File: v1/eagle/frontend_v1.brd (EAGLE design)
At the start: 100 x 50 mm, 57 parts, among them IC1 TINY24/44/84-SSU, IC2 AD5339MSOP8, IC3 LM4041A12DCK, Q10 TIP42C, Q9 TIP41C, T3 TIP35CVERTICAL, T4 TIP35CVERTICAL, U2 LM35DT, U3 LM35DT

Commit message: minor changes
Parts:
- R1, R16, R17, R35: device rcl:R2010 -> rcl:R2512
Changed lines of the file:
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@@
 </autorouter>
 <elements>
-<element name="R1" library="rcl" package="R2010" value="0.1" x="66.5" y="30.5" smashed="yes" rot="R180">
+<element name="R1" library="rcl" package="R2512" value="0.1" x="66.5" y="30.5" smashed="yes" rot="R180">
 <attribute name="NAME" x="65.675" y="28.845" size="1.27" layer="25" rot="R180"/>
 </element>
@@
 <attribute name="NAME" x="67.92" y="6.7048" size="1.27" layer="25" ratio="10"/>
 </element>
-<element name="R16" library="rcl" package="R2010" value="0.1" x="76.25" y="5" rot="R180"/>
-<element name="R17" library="rcl" package="R2010" value="0.1" x="30.25" y="4.75" rot="R180"/>
+<element name="R16" library="rcl" package="R2512" value="0.1" x="76.25" y="5" smashed="yes" rot="R180">
+<attribute name="NAME" x="78.79" y="3.095" size="1.27" layer="25" rot="R180"/>
+</element>
+<element name="R17" library="rcl" package="R2512" value="0.1" x="30.25" y="4.75" smashed="yes" rot="R180">
+<attribute name="NAME" x="32.79" y="2.845" size="1.27" layer="25" rot="R180"/>
+</element>
 <element name="T5" library="transistor" package="SOT23-BEC" value="" x="42.46" y="33.5" smashed="yes" rot="R270">
 <attribute name="NAME" x="38.845" y="32.865" size="1.27" layer="25"/>
@@
 <element name="U2" library="parts" package="TO220AV" value="LM35DT" x="27" y="14.25" rot="R180"/>
 <element name="U3" library="parts" package="TO220AV" value="LM35DT" x="73" y="14.25" rot="R180"/>
-<element name="R35" library="rcl" package="R2010" value="0.1" x="66.5" y="35.25" smashed="yes" rot="R180">
+<element name="R35" library="rcl" package="R2512" value="0.1" x="66.5" y="35.25" smashed="yes" rot="R180">
 <attribute name="NAME" x="66.425" y="38.095" size="1.27" layer="25" rot="R180"/>
 </element>
@@
 <contactref element="O2" pad="8"/>
 <contactref element="C22" pad="1"/>
-<wire x1="64.3" y1="30.5" x2="64.3" y2="35.25" width="1.5" layer="1"/>
-<wire x1="64.3" y1="35.25" x2="65.775" y2="36.725" width="1.5" layer="1"/>
-<wire x1="65.775" y1="36.725" x2="71.525" y2="42.475" width="1.5" layer="1"/>
-<wire x1="71.525" y1="42.475" x2="73.13" y2="44.08" width="1.5" layer="1"/>
-<wire x1="73.13" y1="44.08" x2="73.13" y2="44.5" width="1.5" layer="1"/>
+<wire x1="63.7" y1="30.5" x2="63.7" y2="35.25" width="2" layer="1"/>
+<wire x1="65.775" y1="36.725" x2="71.525" y2="42.475" width="2" layer="1"/>
+<wire x1="71.525" y1="42.475" x2="73.13" y2="44.08" width="2" layer="1"/>
+<wire x1="73.13" y1="44.08" x2="73.13" y2="44.5" width="2" layer="1"/>
 <wire x1="59.46" y1="30.46" x2="59.5" y2="30.5" width="1.5" layer="1"/>
-<wire x1="59.5" y1="30.5" x2="64.3" y2="30.5" width="1.5" layer="1"/>
+<wire x1="59.5" y1="30.5" x2="63.7" y2="30.5" width="2" layer="1"/>
 <wire x1="33.31" y1="29.44" x2="35.75" y2="31.88" width="0.4" layer="16"/>
 <wire x1="35.75" y1="31.88" x2="35.75" y2="32.05" width="0.4" layer="16"/>
@@
 <wire x1="47.25" y1="37" x2="51.45" y2="41.2" width="0.4" layer="1"/>
 <wire x1="51.45" y1="41.2" x2="59.5" y2="41.2" width="0.4" layer="1"/>
+<wire x1="65.775" y1="36.725" x2="64.3" y2="35.25" width="2" layer="1"/>
+<wire x1="64.3" y1="35.25" x2="63.7" y2="35.25" width="1.5" layer="1"/>
 </signal>
 <signal name="VREF">
@@
 <contactref element="HDR_OUT" pad="3"/>
 <contactref element="R5" pad="1"/>
-<wire x1="69.65" y1="5" x2="74.05" y2="5" width="1.5" layer="1"/>
-<wire x1="24.15" y1="4.75" x2="28.05" y2="4.75" width="1.5" layer="1"/>
-<wire x1="96.5" y1="11.46" x2="87.04" y2="2" width="1.5" layer="1"/>
-<wire x1="87.04" y1="2" x2="74.25" y2="2" width="1.5" layer="1"/>
-<wire x1="74.25" y1="2" x2="30.5" y2="2" width="1.5" layer="1"/>
-<wire x1="30.5" y1="2" x2="28.05" y2="4.45" width="1.5" layer="1"/>
-<wire x1="28.05" y1="4.45" x2="28.05" y2="4.75" width="1.5" layer="1"/>
-<wire x1="74.05" y1="5" x2="74.25" y2="4.8" width="1.5" layer="1"/>
-<wire x1="74.25" y1="4.8" x2="74.25" y2="2" width="1.5" layer="1"/>
+<wire x1="69.65" y1="5" x2="73.45" y2="5" width="2" layer="1"/>
+<wire x1="24.15" y1="4.75" x2="27.45" y2="4.75" width="2" layer="1"/>
+<wire x1="96.5" y1="11.46" x2="87.04" y2="1.75" width="2" layer="1"/>
+<wire x1="87.04" y1="1.75" x2="73.5" y2="1.75" width="2" layer="1"/>
+<wire x1="73.5" y1="1.75" x2="30.75" y2="1.75" width="2" layer="1"/>
+<wire x1="30.75" y1="1.75" x2="28.05" y2="4.45" width="2" layer="1"/>
+<wire x1="28.05" y1="4.45" x2="27.45" y2="4.75" width="1.5" layer="1"/>
 <wire x1="28.25" y1="41.2" x2="26.7" y2="41.2" width="0.4" layer="1"/>
 <wire x1="26.7" y1="41.2" x2="23.5" y2="38" width="0.4" layer="1"/>
@@
 <wire x1="19.3" y1="30.05" x2="19" y2="29.75" width="0.4" layer="16"/>
 <wire x1="19" y1="29.75" x2="19" y2="9.25" width="0.4" layer="16"/>
+<wire x1="73.45" y1="5" x2="73.5" y2="4.95" width="1.5" layer="1"/>
+<wire x1="73.5" y1="4.95" x2="73.5" y2="1.75" width="2" layer="1"/>
 </signal>
 <signal name="N$29">
@@
 <contactref element="T4" pad="P3"/>
 <contactref element="R16" pad="1"/>
-<wire x1="78.45" y1="10.55" x2="78.45" y2="5" width="1.5" layer="1"/>
+<wire x1="78.45" y1="10.55" x2="79.05" y2="9.95" width="2" layer="1"/>
+<wire x1="79.05" y1="9.95" x2="79.05" y2="5" width="2" layer="1"/>
 </signal>
 <signal name="N$19">
 <contactref element="T3" pad="P3"/>
 <contactref element="R17" pad="1"/>
-<wire x1="32.45" y1="4.75" x2="32.45" y2="10.55" width="1.5" layer="1"/>
+<wire x1="33.05" y1="4.75" x2="33.05" y2="9.95" width="1.5" layer="1"/>
+<wire x1="33.05" y1="9.95" x2="32.45" y2="10.55" width="1.5" layer="1"/>
 </signal>
 <signal name="N$15">
@@
 <contactref element="R12" pad="1"/>
 <contactref element="T4" pad="P2"/>
-<wire x1="68.7" y1="35.25" x2="68.7" y2="33.25" width="1.5" layer="1"/>
-<wire x1="68.7" y1="33.25" x2="68.7" y2="30.5" width="1.5" layer="1"/>
-<wire x1="73" y1="10.55" x2="69.95" y2="7.5" width="1.5" layer="1"/>
-<wire x1="69.95" y1="7.5" x2="66.25" y2="7.5" width="1.5" layer="1"/>
-<wire x1="66.25" y1="7.5" x2="64.5" y2="9.25" width="1.5" layer="1"/>
-<wire x1="64.5" y1="9.25" x2="64.5" y2="20.25" width="1.5" layer="1"/>
-<wire x1="64.5" y1="20.25" x2="64.5" y2="23.5" width="1.5" layer="1"/>
-<wire x1="64.5" y1="23.5" x2="68.7" y2="27.7" width="1.5" layer="1"/>
-<wire x1="68.7" y1="27.7" x2="68.7" y2="30.5" width="1.5" layer="1"/>
-<wire x1="27" y1="10.55" x2="23.95" y2="7.5" width="1.5" layer="1"/>
-<wire x1="23.95" y1="7.5" x2="20" y2="7.5" width="1.5" layer="1"/>
-<wire x1="20" y1="7.5" x2="18.5" y2="9" width="1.5" layer="1"/>
-<wire x1="18.5" y1="9" x2="18.5" y2="20.25" width="1.5" layer="1"/>
-<wire x1="18.5" y1="20.25" x2="64.5" y2="20.25" width="1.5" layer="1"/>
-<wire x1="72.55" y1="33.25" x2="68.7" y2="33.25" width="0.4" layer="1"/>
+<wire x1="73" y1="10.55" x2="69.95" y2="7.5" width="2" layer="1"/>
+<wire x1="69.95" y1="7.5" x2="66.25" y2="7.5" width="2" layer="1"/>
+<wire x1="66.25" y1="7.5" x2="64.5" y2="9.25" width="2" layer="1"/>
+<wire x1="64.5" y1="9.25" x2="64.5" y2="20.25" width="2" layer="1"/>
+<wire x1="64.5" y1="20.25" x2="64.5" y2="23.5" width="2" layer="1"/>
+<wire x1="27" y1="10.55" x2="23.95" y2="7.5" width="2" layer="1"/>
+<wire x1="23.95" y1="7.5" x2="20" y2="7.5" width="2" layer="1"/>
+<wire x1="20" y1="7.5" x2="18.5" y2="9" width="2" layer="1"/>
+<wire x1="18.5" y1="9" x2="18.5" y2="20.25" width="2" layer="1"/>
+<wire x1="18.5" y1="20.25" x2="64.5" y2="20.25" width="2" layer="1"/>
+<wire x1="69.3" y1="35.25" x2="69.3" y2="33.25" width="2" layer="1"/>
+<wire x1="69.3" y1="33.25" x2="69.3" y2="30.5" width="2" layer="1"/>
+<wire x1="72.55" y1="33.25" x2="69.3" y2="33.25" width="0.3" layer="1"/>
+<wire x1="64.5" y1="23.5" x2="69.3" y2="28.3" width="2" layer="1"/>
+<wire x1="69.3" y1="28.3" x2="69.3" y2="30.5" width="2" layer="1"/>
 </signal>
 <signal name="ADC1">

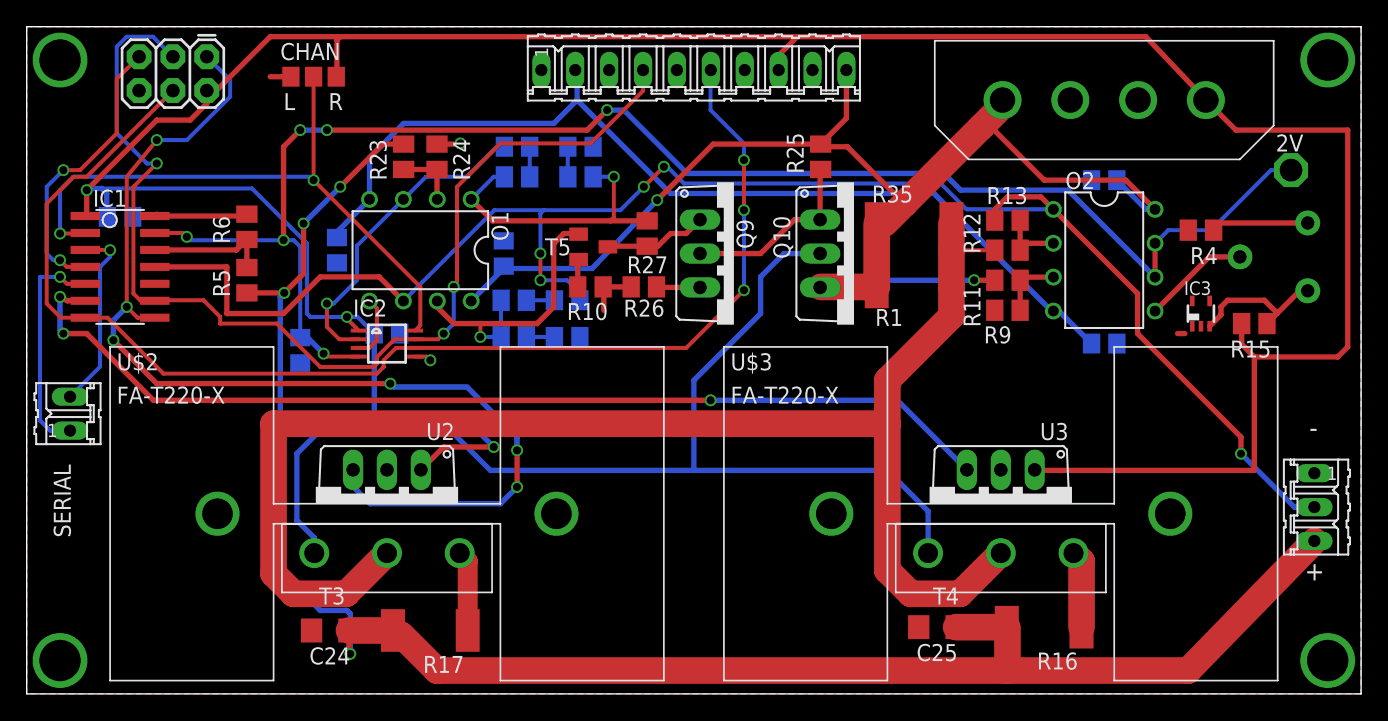
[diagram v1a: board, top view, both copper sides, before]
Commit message: slight changes for board house
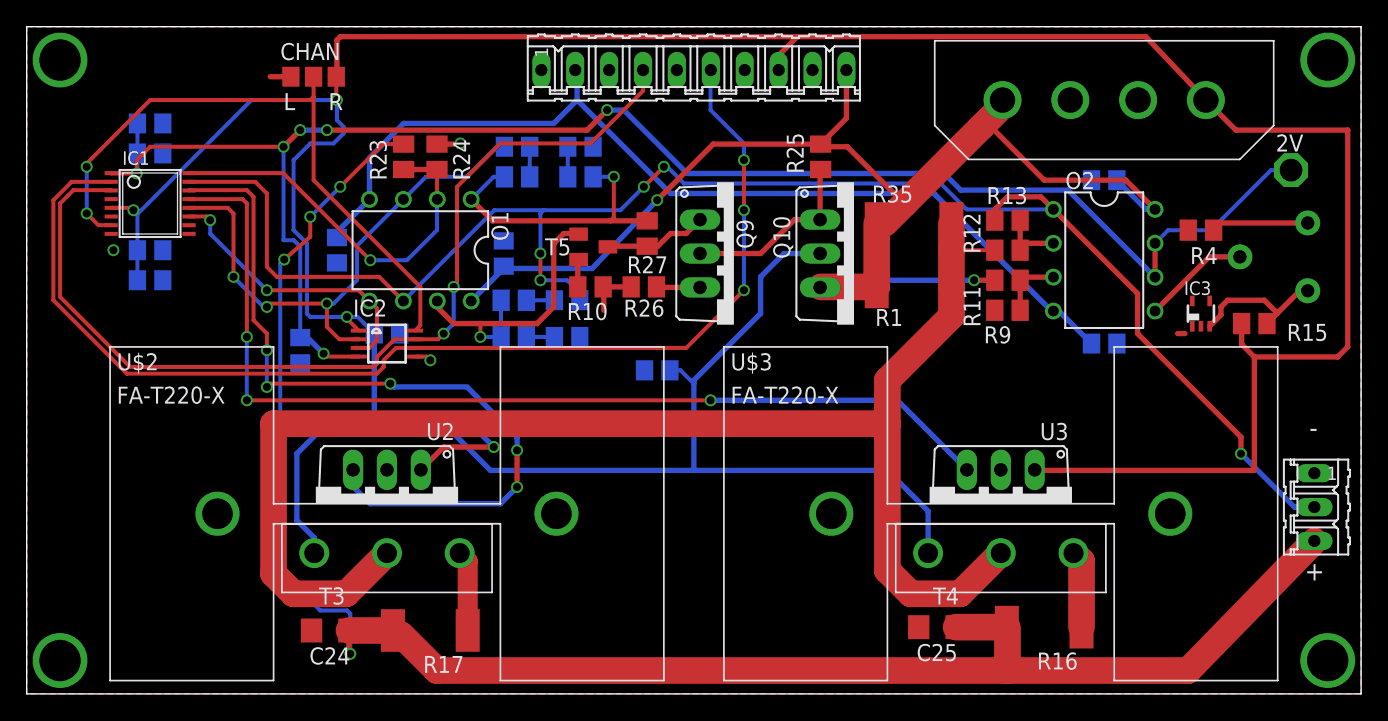
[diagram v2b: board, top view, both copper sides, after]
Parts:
- removed HEADER_ICSP: AVR_SPI_PRG_6PTH, SparkFun-Connectors:2X3
- removed R5: 5k, rcl:M0805
- removed R6: 1k, rcl:M0805
- removed SERIAL: (no value), con-amp-quick:02P
- added C10, C8: 1u, rcl:C0805
- added C11, C9: 0.1u, rcl:C0805
- C1, C2, C3: value (none) -> 0.1u
- IC1: value TINY24/44/84-SSU -> ADC128D818; device avr-7:SOIC14 -> parts:TSSOP16
- R23: value 6.2k 0.1% -> 4k 0.1%
- R24: value 1.3k 0.1% -> 1k 0.1%
- moved C1 5.26 mm to (9.25, 31.0)
- moved IC1 5.26 mm to (9.25, 36.8)
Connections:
- removed net ADC1: IC1.12, R5.2, R6.1
- removed net ADC3: IC1.10
- removed net N$10: IC1.3, SERIAL.2
- removed net N$11: IC1.5, SERIAL.1
- removed net N$29: O1.2, R23.2, R24.1
- removed net RESET: HEADER_ICSP.5, IC1.4
- new net VFEEDBACK: IC1.16, O1.2, R23.2, R24.1
- net +5V: now also C8.1, IC1.5; no longer HEADER_ICSP.2, IC1.1
- net CHANNEL_SELECT: now also IC1.7; no longer IC1.2
- net GNDA: now also C10.2, C11.2, C8.2, C9.2, IC1.4, IC1.8; no longer HEADER_ICSP.6, IC1.14, R6.2
- net I_CONTROL: now also IC1.11
- net I_SENSE: now also IC1.15; no longer IC1.11
- net SCL: now also IC1.3; no longer HEADER_ICSP.3, IC1.9
- net SDA: now also IC1.2; no longer HEADER_ICSP.4, IC1.7
- net TEMP_1: now also IC1.14; no longer HEADER_ICSP.1, IC1.8
- net TEMP_2: now also IC1.13; no longer IC1.6
- net VDD: now also C10.1, C9.1, IC1.1; no longer IC1.13
- net VOUT: no longer R5.1
- net VREF: now also C11.1
- net V_CONTROL: now also IC1.12
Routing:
- net VFEEDBACK: track 0.00 -> 29.3 mm, vias 0 -> 1
- net TEMP_1: track 80.8 -> 58.6 mm, vias 6 -> 5
- net RESET: track 21.7 -> 0.00 mm, vias 2 -> 0
- net N$11: track 16.9 -> 0.00 mm, vias 1 -> 0
- net I_CONTROL: track 4.77 -> 21.5 mm, vias 0 -> 2
- net V_CONTROL: track 24.2 -> 40.5 mm, vias 1 -> 3
- net N$10: track 14.1 -> 0.00 mm, vias 1 -> 0
- net SCL: track 83.1 -> 73.4 mm, vias 3 -> 2
- net ADC1: track 9.32 -> 0.00 mm
- net SDA: track 95.3 -> 86.9 mm
- net VDD: track 116.7 -> 125.0 mm
- net GNDA: track 16.4 -> 9.28 mm, vias 2 -> 3
- net +5V: track 217.6 -> 212.1 mm, vias 3 -> 4
- net N$29: track 4.75 -> 0.00 mm
- net VOUT: track 135.6 -> 132.9 mm
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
